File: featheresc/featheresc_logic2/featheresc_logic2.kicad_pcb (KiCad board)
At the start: 2 copper layers, 92 x 39 mm, 48 parts, among them J1 RC IN 1, J2 RC IN 2, J3 soicbite prog connector, J7 Interconnect 1, J8 Interconnect 2, U1 AMS1117-50, U2 XL1509-ADJE1, U3 ATtiny1614-SS, U4 NCP81155MN, U5 NCP81155MN, U6 NCP81155MN, U7 NCP81155MN, U8 78L12G-AB3-R

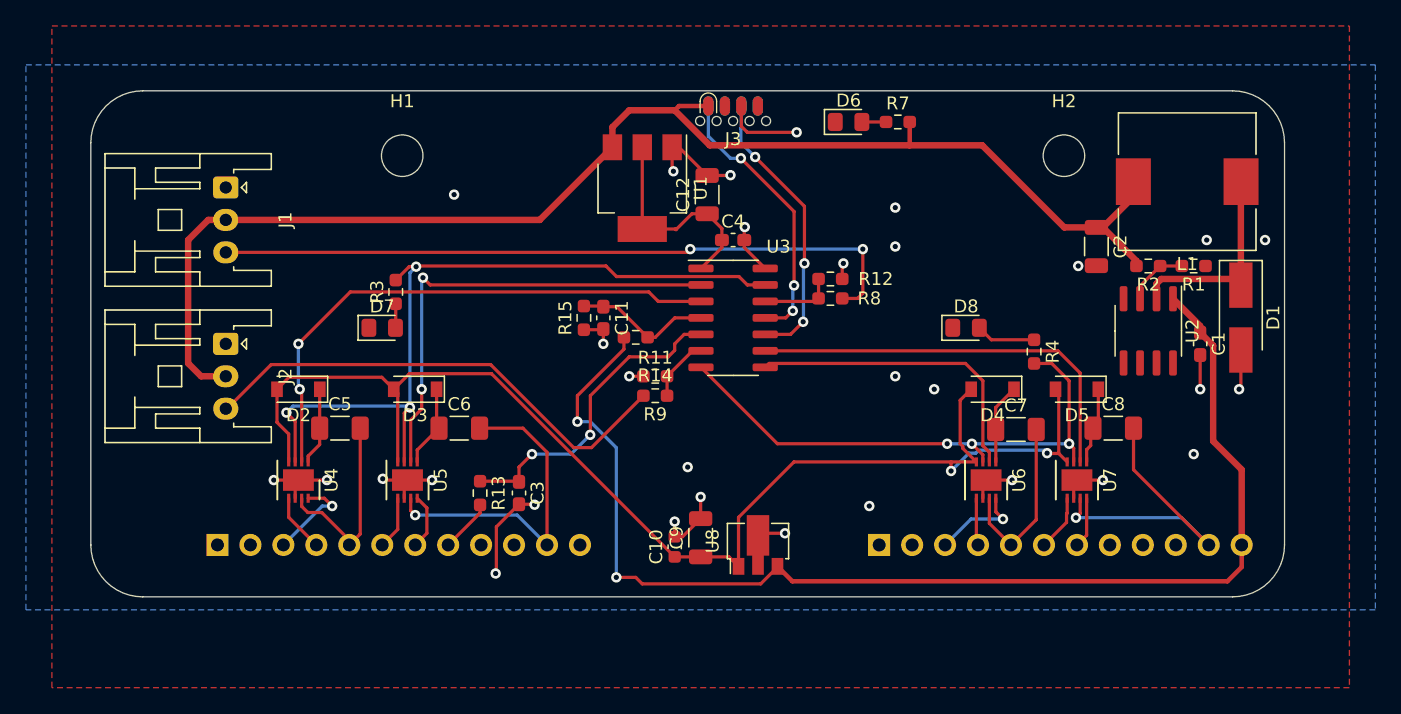
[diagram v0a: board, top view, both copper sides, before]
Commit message: Update layout to be more compact, swap a few parts
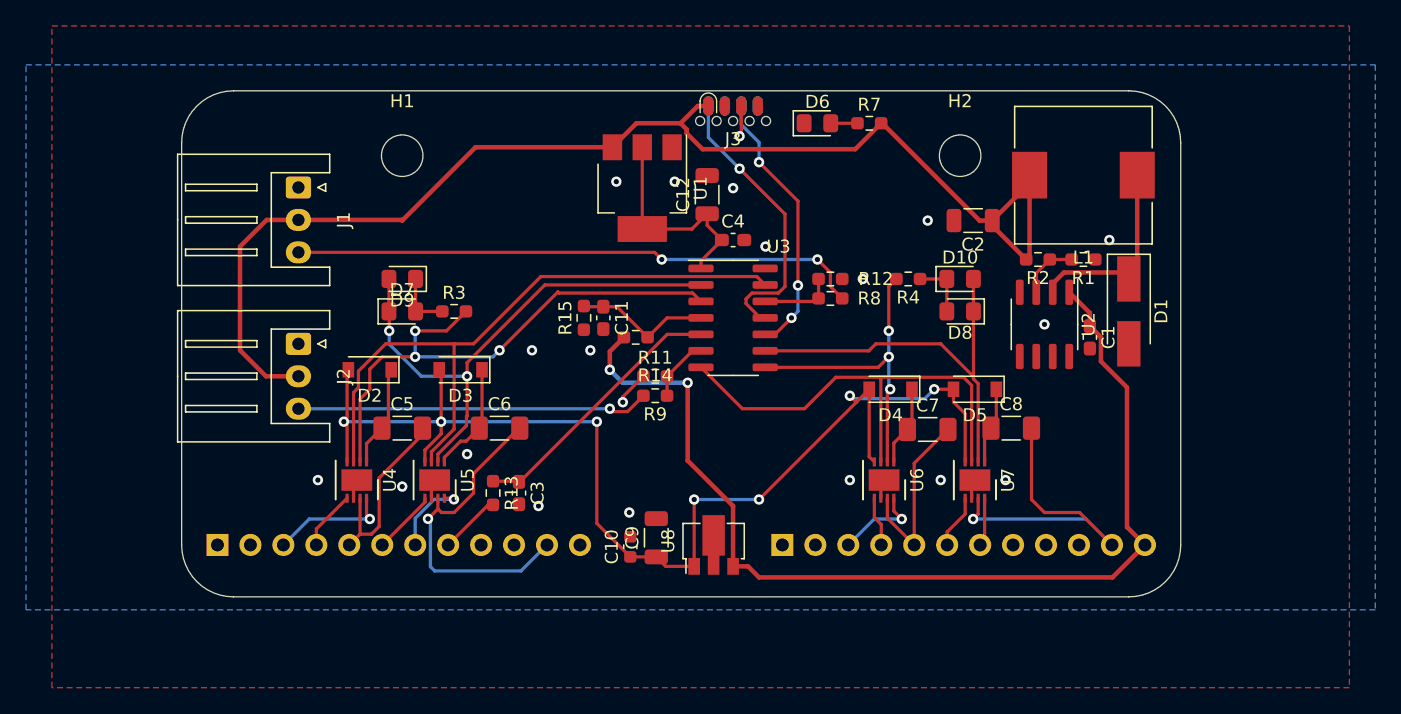
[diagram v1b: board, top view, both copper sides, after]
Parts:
- added D10: Green, LED_SMD:LED_0805_2012Metric_Pad1.15x1.40mm_HandSolder, F.Cu at (171.0, 74.5)
- added D9: Green, LED_SMD:LED_0805_2012Metric_Pad1.15x1.40mm_HandSolder, F.Cu at (128.0, 74.5)
- J1, J2: footprint Connector_JST:JST_XA_S03B-XASK-1_1x03_P2.50mm_Horizontal -> Connector_JST:JST_XH_S3B-XH-A_1x03_P2.50mm_Horizontal
- moved R4 11.2 mm to (167.0, 74.5), turned to 180 degrees
- moved C2 9.71 mm to (172.0, 70.0), turned to 180 degrees
- moved D1 8.65 mm to (184.0, 77.0)
- moved C1 8.51 mm to (181.0, 79.0)
- moved R1 8.51 mm to (180.5, 73.0)
- moved R2 8.51 mm to (177.0, 73.0)
- moved L1 8.02 mm to (180.5, 66.5)
- moved U2 8.02 mm to (177.5, 78.0)
- moved H2 8.00 mm to (171.0, 65.0)
- moved C8 7.86 mm to (174.9, 86.0)
- moved D4 7.86 mm to (165.6, 83.0)
- moved D5 7.86 mm to (172.1, 83.0)
- moved U6 7.86 mm to (165.1, 90.0)
- moved U7 7.86 mm to (172.1, 90.0)
- moved J8 7.46 mm to (157.3, 95.0)
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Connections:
- D7 pad 1: GND -> /MOTORR_1
- D8 pad 1: GND -> /MOTORR_2
- R3 pad 2: /MOTOREN_1 -> /MOTORF_1
- R4 pad 2: /MOTOREN_2 -> /MOTORF_2
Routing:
- net GND: track 63.0 -> 11.1 mm, vias 31 -> 20
- net VBAT: track 94.6 -> 80.0 mm
- net /RXIN_2: track 37.8 -> 27.2 mm, vias 0 -> 1
- net /RXIN_1: track 54.4 -> 44.0 mm
- net /MOTOREN_1: track 58.8 -> 51.6 mm, vias 3 -> 0
- net VBEC: track 105.2 -> 98.3 mm
- net +12V: track 100.8 -> 94.0 mm, vias 2 -> 7
- net /MOTOREN_2: track 42.2 -> 35.9 mm, vias 3 -> 0
- net /MOTORR_1: track 36.2 -> 41.1 mm
- net /ISENSE_IN: track 24.5 -> 20.8 mm, vias 2 -> 0
- net Net-(D7-Pad2): track 1.86 -> 4.56 mm
- net /PHASE22: track 24.1 -> 26.4 mm
- net /gatedrivers1/BOOST2: track 6.37 -> 8.56 mm
- net /GATEH21: track 4.28 -> 6.42 mm, vias 0 -> 1
- net /GATEH11: track 7.10 -> 9.19 mm
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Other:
- board size 92 x 39 mm -> 77 x 39 mm

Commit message: Silkscreen etc
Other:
- board text added: "+5"
- board text added: "+5V"
- board text added: "@markxr 2022"
- board text added: "GND"
- board text added: "MOTOR1 ACTIVE"
- board text added: "MOTOR2 ACTIVE"
- board text added: "POWER ON"
- board text added: "SIG"

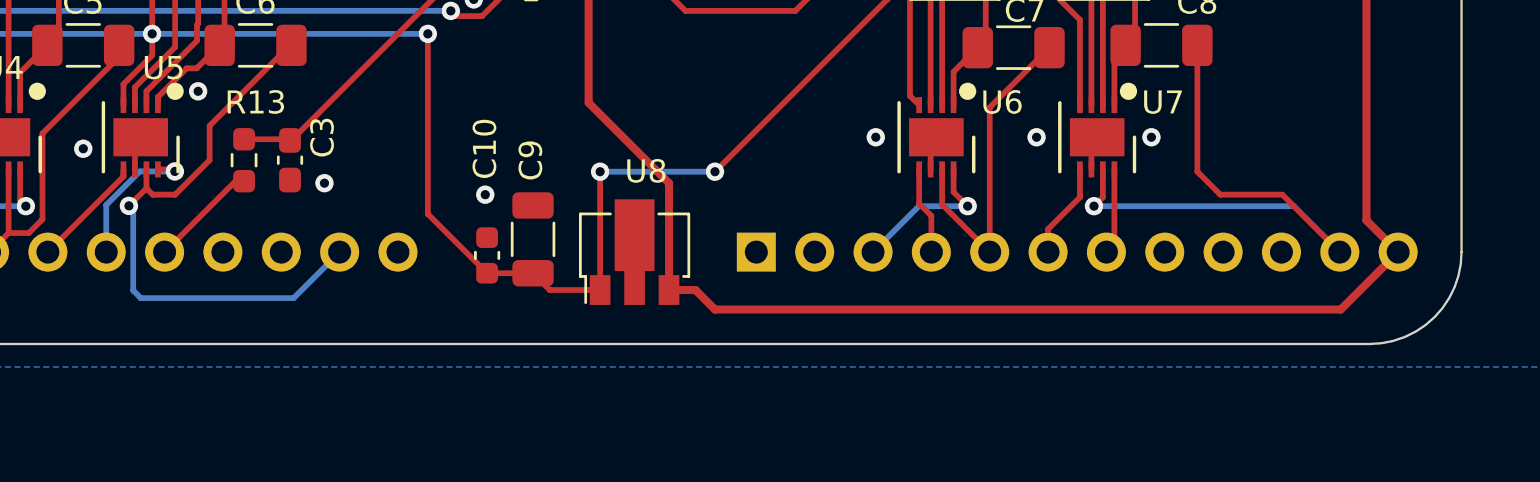
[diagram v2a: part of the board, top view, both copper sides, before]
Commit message: improve interconnect pinouts
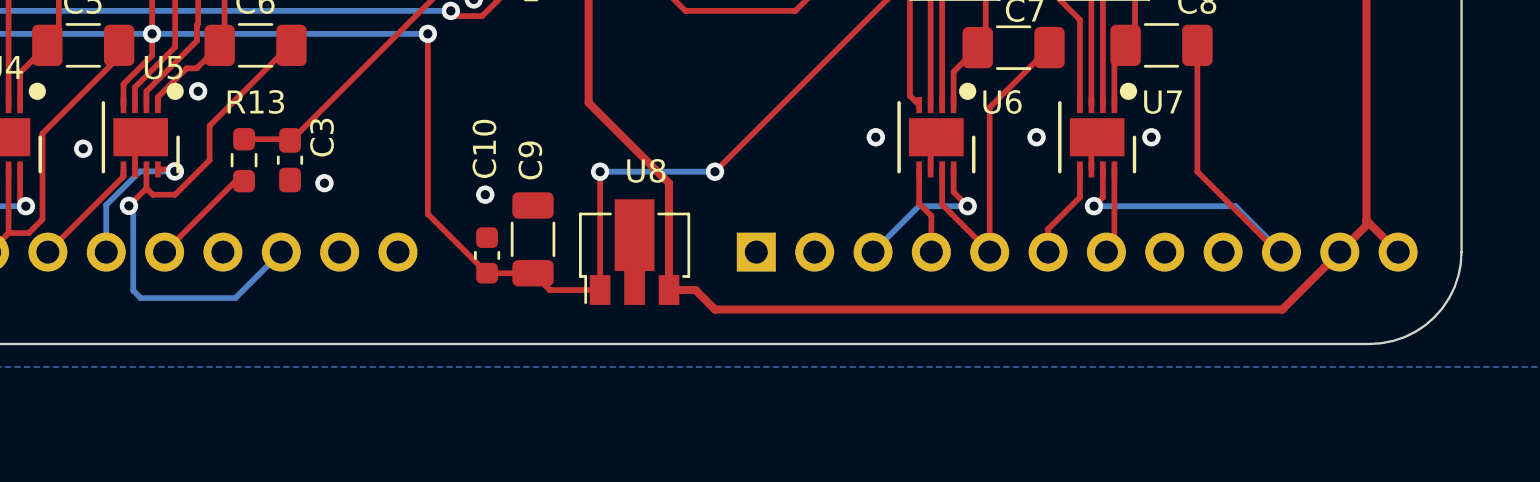
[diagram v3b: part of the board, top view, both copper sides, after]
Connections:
- J7 pad 10: unconnected-(J7-Pad10) -> /PHASE21
- J7 pad 11: /PHASE21 -> unconnected-(J7-Pad11)
- J7 pad 2: unconnected-(J7-Pad2) -> GND
- J8 pad 10: unconnected-(J8-Pad10) -> /PHASE22
- J8 pad 11: /PHASE22 -> VBAT
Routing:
- net /PHASE22: track 26.4 -> 21.4 mm
- net /PHASE21: track 25.6 -> 23.1 mm
- net VBAT: track 80.0 -> 79.3 mm

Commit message: Mixing switch
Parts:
- added R5: 33k, Resistor_SMD:R_0603_1608Metric_Pad0.98x0.95mm_HandSolder, F.Cu at (133.5, 67.2)
- added SW1: SW_DIP_x01, Button_Switch_THT:SW_DIP_SPSTx01_Slide_6.7x4.1mm_W7.62mm_P2.54mm_LowProfile, F.Cu at (141.0, 63.0)
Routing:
- net /TXDEBUG: track 22.0 -> 33.4 mm
- net Net-(R5-Pad1): track 0.00 -> 3.39 mm
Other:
- board text added: "MIX EN"
